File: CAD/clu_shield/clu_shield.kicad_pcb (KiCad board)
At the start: 2 copper layers, 95 x 70 mm, 39 parts, among them J1 Conn_01x28_Pin, J2 Conn_01x02_Pin, J3 Conn_01x02_Pin, SW1 ERD516RSZ, SW10 SW_SPDT, SW11 SW_SPDT, SW12 SW_SPDT, SW13 SW_SPDT, SW2 ERD516RSZ, SW3 ERD516RSZ, SW4 ERD516RSZ, SW5 ERD508RSZ, SW6 SW_SPDT, SW7 SW_SPDT, SW8 SW_SPDT, SW9 SW_SPDT

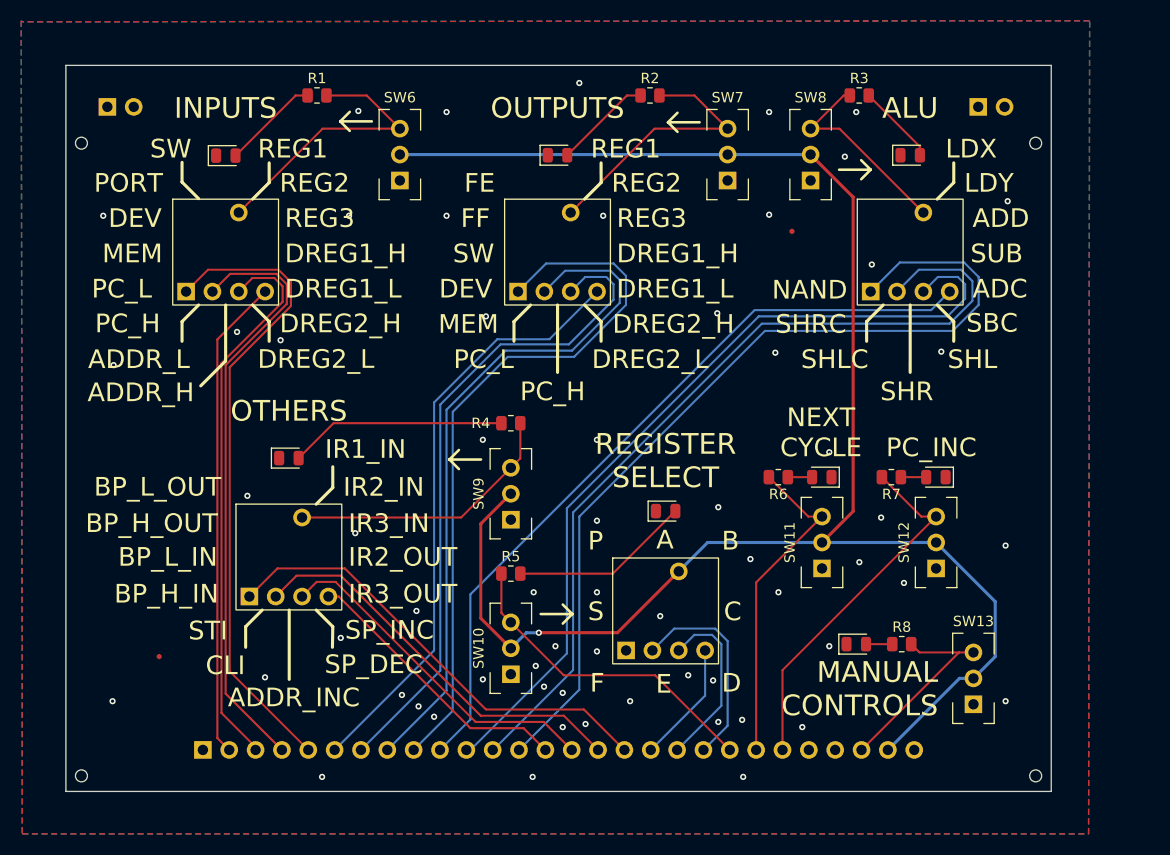
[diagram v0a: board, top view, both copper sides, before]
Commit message: CLU Controls Shield layout changes, add reg2 select switch, CLU layout changes
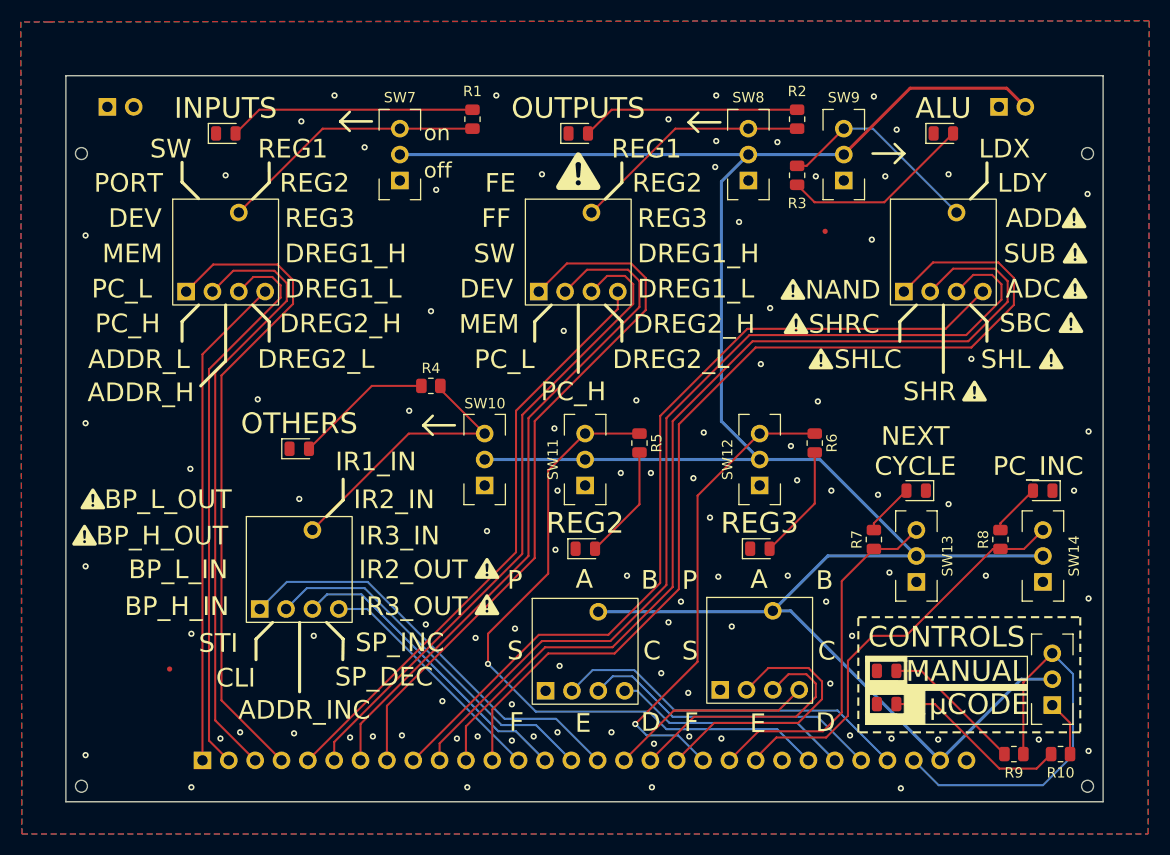
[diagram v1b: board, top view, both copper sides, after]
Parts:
- added D10: LED, LED_SMD:LED_0805_2012Metric, F.Cu at (157.8, 91.7)
- added D5: LED, LED_SMD:LED_0805_2012Metric, F.Cu at (128.8, 76.7)
- added G***: LOGO, 8-bit_computer:warning_symbol, F.Cu at (151.5, 58.4)
- added G***: LOGO, 8-bit_computer:warning_symbol, F.Cu at (166.3, 61.5)
- added G***: LOGO, 8-bit_computer:warning_symbol, F.Cu at (176.0, 48.2)
- added G***: LOGO, 8-bit_computer:warning_symbol, F.Cu at (175.9, 44.8)
- added G***: LOGO, 8-bit_computer:warning_symbol, F.Cu at (175.6, 54.9)
- added G***: LOGO, 8-bit_computer:warning_symbol, F.Cu at (148.8, 51.7)
- added G***: LOGO, 8-bit_computer:warning_symbol, F.Cu at (119.3, 78.6)
- added G***: LOGO, 8-bit_computer:warning_symbol, F.Cu at (176.0, 51.6)
- added G***: LOGO, 8-bit_computer:warning_symbol, F.Cu at (81.3, 71.9)
- added G***: LOGO, LOGO, F.Cu at (128.1, 40.3)
- added G***: LOGO, 8-bit_computer:warning_symbol, F.Cu at (80.5, 75.4)
- added G***: LOGO, 8-bit_computer:warning_symbol, F.Cu at (173.7, 58.4)
- added G***: LOGO, 8-bit_computer:warning_symbol, F.Cu at (149.1, 55.0)
- added G***: LOGO, 8-bit_computer:warning_symbol, F.Cu at (119.3, 82.1)
- added R10: 1k, Resistor_SMD:R_0805_2012Metric, F.Cu at (174.6, 96.5)
- added R5: 1k, Resistor_SMD:R_0805_2012Metric, F.Cu at (134.0, 66.5)
- added SW11: SW_SPDT, 8-bit_computer:SW_Slide_SPDT_8.5x3.8mm, F.Cu at (128.8, 68.1)
- added SW5: ERD508RSZ, 8-bit_computer:ERD5XXXS, F.Cu at (128.8, 86.6)
- J1: value Conn_01x28_Pin -> Conn_01x30_Pin; footprint Connector_PinHeader_2.54mm:PinHeader_1x28_P2.54mm_Vertical -> Connector_PinHeader_2.54mm:PinHeader_1x30_P2.54mm_Vertical
- moved Ref** 49.2 mm to (103.9, 90.1)
- moved R6 31.9 mm to (150.9, 66.5), turned to -90 degrees
- moved SW12 30.1 mm to (145.6, 68.1)
- moved R1 15.2 mm to (117.9, 35.3), turned to -90 degrees
- moved R9 15.1 mm to (170.1, 96.5)
- moved R2 14.4 mm to (149.2, 35.3), turned to -90 degrees
- moved R8 12.1 mm to (168.8, 75.8), turned to 90 degrees
- moved R7 11.0 mm to (156.6, 75.8), turned to 90 degrees
- moved SW14 10.4 mm to (172.9, 77.4)
- moved D8 10.4 mm to (172.9, 71.1)
- moved SW6 9.83 mm to (145.6, 86.5)
- moved D6 9.78 mm to (145.6, 76.7)
- moved R3 9.75 mm to (149.2, 40.7), turned to -90 degrees
- moved SW13 9.19 mm to (160.7, 77.4)
- moved D7 9.19 mm to (160.7, 71.1)
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- renumbered D5 to D6, D6 to D7, D7 to D8, D8 to D9, R5 to R6, R6 to R7, R7 to R8, R8 to R9, SW9 to SW10, SW10 to SW12, SW11 to SW13, SW12 to SW14, SW13 to SW15, SW5 to SW6, SW6 to SW7, SW7 to SW8, SW8 to SW9
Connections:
- D7 pad 2: Net-(D6-A) (its old number) -> Net-(D7-A)
- D8 pad 2: Net-(D7-A) -> Net-(D8-A)
- J1 pad 1: GND -> /sig1.0
- J1 pad 10: /sig2.0 -> /sig2.1
- J1 pad 11: /sig2.1 -> /sig2.2
- J1 pad 12: /sig2.2 -> /sig2.3
- J1 pad 13: /sig2.3 -> /sig2.4
- J1 pad 14: /sig2.4 -> /sig2.5
- J1 pad 15: /sig2.5 -> /sig2.6
- J1 pad 16: /sig2.6 -> /sig2.7
- J1 pad 17: /sig2.7 -> /sig3.0
- J1 pad 18: /sig3.0 -> /sig3.1
- J1 pad 19: /sig3.1 -> /sig3.2
- J1 pad 2: /sig1.0 -> /sig1.1
- J1 pad 20: /sig3.2 -> /sig3.3
- J1 pad 21: /sig3.3 -> /sig3.4
- J1 pad 22: /sig3.4 -> /sig3.5
- J1 pad 23: /sig3.5 -> /sig3.6
- J1 pad 24: /sig3.6 -> /sig3.7
- J1 pad 25: /sig3.7 -> /reg2_sig.0
- J1 pad 26: man_ctrl -> /reg2_sig.1
- J1 pad 27: +5V -> /reg2_sig.2
- J1 pad 28: GND -> man_ctrl
- J1 pad 3: /sig1.1 -> /sig1.2
- J1 pad 4: /sig1.2 -> /sig1.3
- J1 pad 5: /sig1.3 -> /sig1.4
- J1 pad 6: /sig1.4 -> /sig1.5
- J1 pad 7: /sig1.5 -> /sig1.6
- J1 pad 8: /sig1.6 -> /sig1.7
- J1 pad 9: /sig1.7 -> /sig2.0
- J3 pad 2: GND -> +5V
- R7 pad 1: Net-(D6-A) (its old number) -> /sig3.4
- R7 pad 2: /sig3.4 -> Net-(D7-A)
- R8 pad 1: Net-(D7-A) -> /sig3.5
- R8 pad 2: /sig3.5 -> Net-(D8-A)
- SW15 pad 1: unconnected-(SW13-A-Pad1) (its old number) -> /ucode_ctrl
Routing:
- net /sig3.7: track 0.00 -> 66.1 mm, vias 0 -> 1
- net +5V: track 169.9 -> 222.4 mm, vias 1 -> 0
- net /reg2_sig.2: track 0.00 -> 34.9 mm
- net /reg2_sig.1: track 0.00 -> 29.3 mm
- net /reg2_sig.0: track 0.00 -> 23.0 mm
- net man_ctrl: track 19.6 -> 39.1 mm
- net Net-(D10-A): track 0.00 -> 18.1 mm
- net /sig3.3: track 31.3 -> 46.3 mm, vias 0 -> 1
- net Net-(D1-A): track 9.34 -> 23.8 mm
- net Net-(D2-A): track 9.45 -> 21.1 mm
- net Net-(D9-A): track 2.53 -> 13.8 mm
- net Net-(D5-A): track 0.00 -> 11.0 mm
- net Net-(D3-A): track 7.81 -> 18.5 mm
- net /sig2.1: track 80.6 -> 89.8 mm
- net /sig2.2: track 83.6 -> 92.7 mm
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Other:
- board size 95 x 70 mm -> 100 x 70 mm
- board text added: "CONTROLS"
- board text added: "MANUAL"
- board text added: "off"
- board text added: "on"
- board text added: "μCODE"
- board text removed: "MANUAL CONTROLS"
- board text removed: "REGISTER SELECT"
